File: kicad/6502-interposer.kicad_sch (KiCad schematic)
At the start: 6 parts, among them J1 LogicAnalyzer #1, J2 LogicAnalyzer #2, J3 Conn_02x09_Odd_Even, U1 65CE02

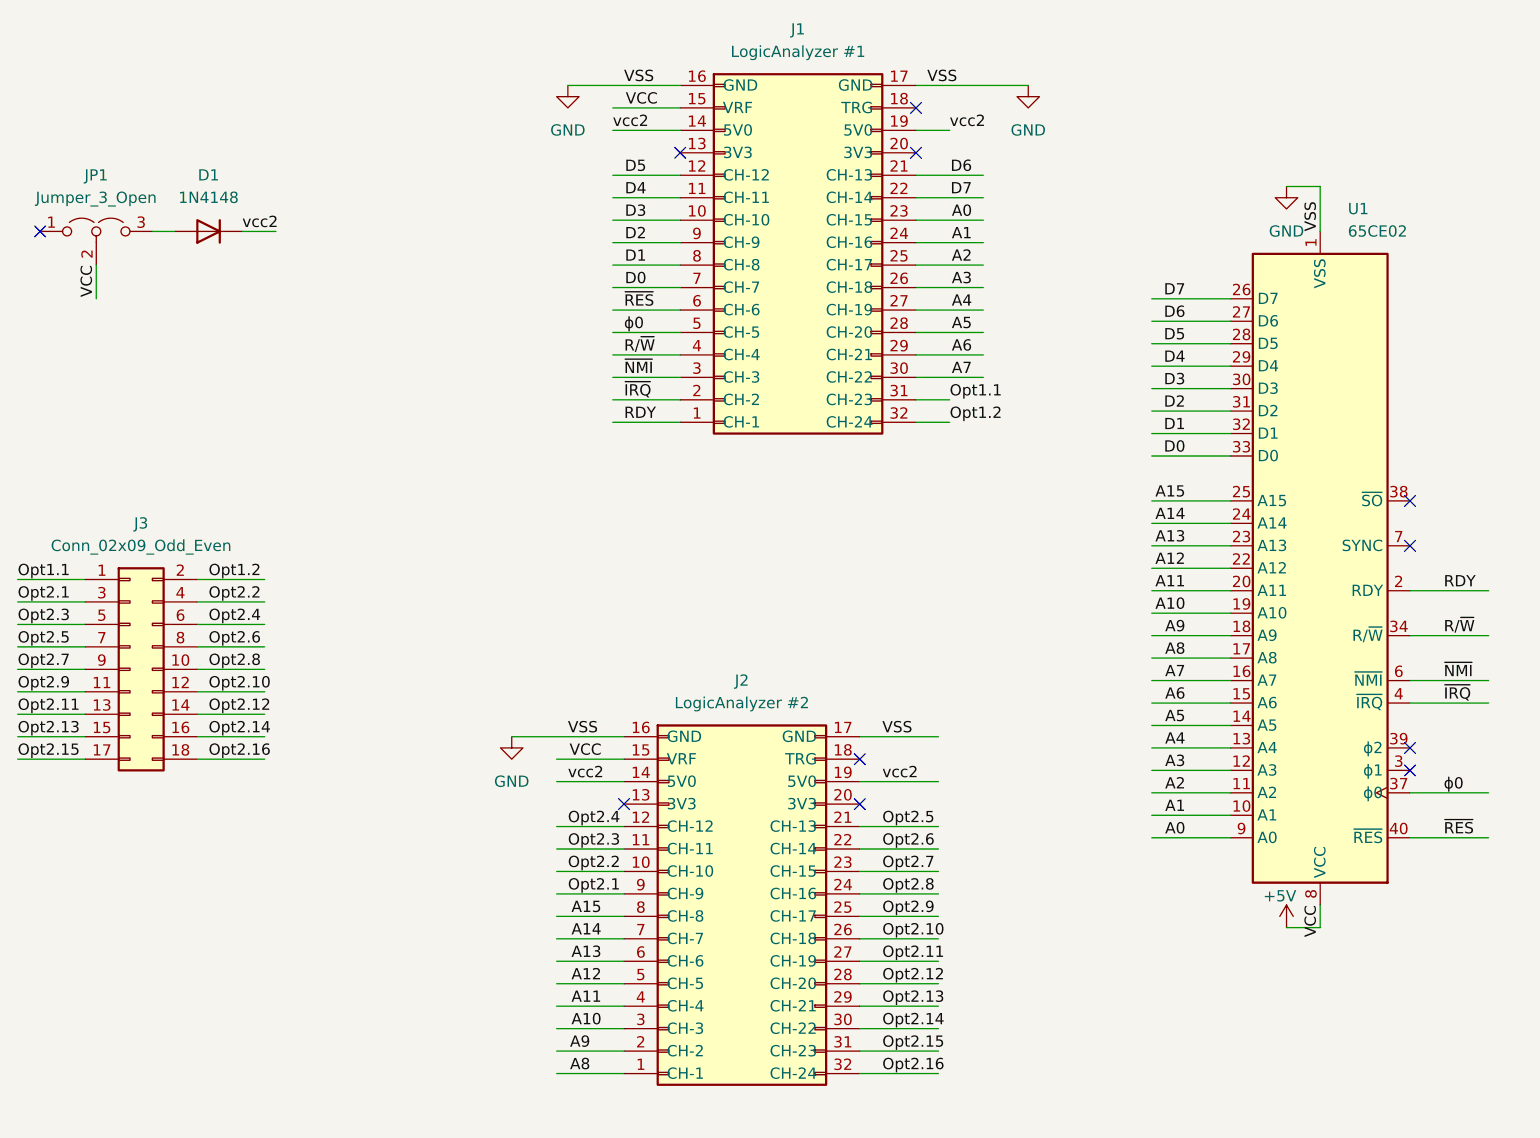
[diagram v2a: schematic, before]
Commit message: Added Phase1 and SYNC
Ended up digging into the 6502 documentation to understand why SYNC and Phase1 are important. Although the IIc and IIe do not use these signals, they do have a function. Sync tells us when the cpu is executing an action, on the system. Phase1 is the inverse of Phase0 or Phase2, and is the time when the Apple II series performs memory actions. Video phase addressing traffic is not visible to the CPU in the Apple II series, the Option ports need to be used to grab those signals. RAn
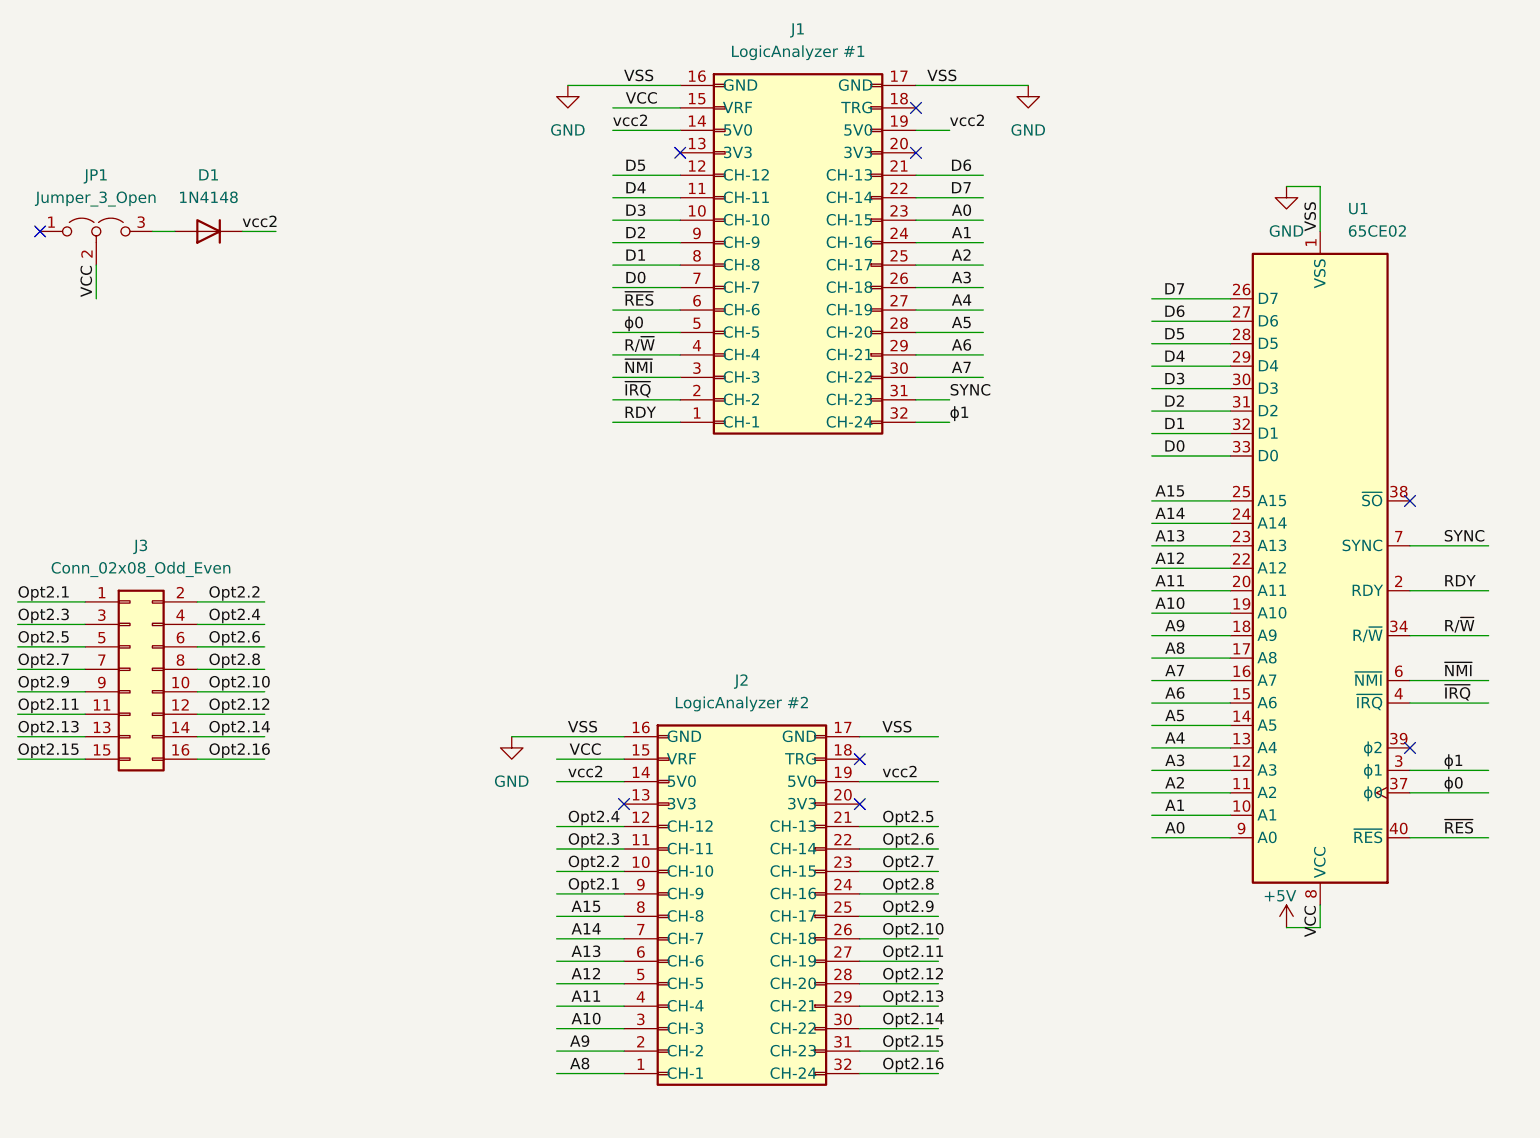
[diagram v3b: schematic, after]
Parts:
- J3: value Conn_02x09_Odd_Even -> Conn_02x08_Odd_Even; footprint Connector_PinSocket_2.54mm:PinSocket_2x09_P2.54mm_Vertical -> Connector_PinSocket_2.54mm:PinSocket_2x08_P2.54mm_Vertical; symbol Connector_Generic:Conn_02x09_Odd_Even -> Connector_Generic:Conn_02x08_Odd_Even
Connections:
- net Opt2.1: now also J3.1 (Pin_1); no longer J3.3 (Pin_3)
- net Opt2.10: now also J3.10 (Pin_10); no longer J3.12 (Pin_12)
- net Opt2.11: now also J3.11 (Pin_11); no longer J3.13 (Pin_13)
- net Opt2.12: now also J3.12 (Pin_12); no longer J3.14 (Pin_14)
- net Opt2.13: now also J3.13 (Pin_13); no longer J3.15 (Pin_15)
- net Opt2.14: now also J3.14 (Pin_14); no longer J3.16 (Pin_16)
- net Opt2.15: now also J3.15 (Pin_15); no longer J3.17 (Pin_17)
- net Opt2.16: now also J3.16 (Pin_16); no longer J3.18 (Pin_18)
- net Opt2.2: now also J3.2 (Pin_2); no longer J3.4 (Pin_4)
- net Opt2.3: now also J3.3 (Pin_3); no longer J3.5 (Pin_5)
- net Opt2.4: now also J3.4 (Pin_4); no longer J3.6 (Pin_6)
- net Opt2.5: now also J3.5 (Pin_5); no longer J3.7 (Pin_7)
- net Opt2.6: now also J3.6 (Pin_6); no longer J3.8 (Pin_8)
- net Opt2.7: now also J3.7 (Pin_7); no longer J3.9 (Pin_9)
- net Opt2.8: now also J3.8 (Pin_8); no longer J3.10 (Pin_10)
- net Opt2.9: now also J3.9 (Pin_9); no longer J3.11 (Pin_11)
- net ϕ1: now reaches U1.3 (ϕ1)
- net ϕ1: now also J1.32 (CH-24)
- net SYNC: now reaches U1.7 (SYNC)
- net SYNC: now also J1.31 (CH-23)
- removed net Opt1.1: J1.31 (CH-23), J3.1 (Pin_1)
- removed net Opt1.2: J1.32 (CH-24), J3.2 (Pin_2)
- no-connect marks 11 -> 9
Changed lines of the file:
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@@
-	)
-	(no_connect
-		(at 201.93 86.36)
 	)
 	(no_connect
@@
 	)
 	(no_connect
-		(at 201.93 111.76)
-	)
-	(no_connect
 		(at 139.7 115.57)
 	)
@@
 	(wire
 		(pts
+			(xy 201.93 86.36) (xy 210.82 86.36)
+		)
+		(stroke
+			(width 0)
+			(type default)
+		)
+	)
+	(wire
+		(pts
 			(xy 64.77 105.41) (xy 72.39 105.41)
 		)
@@
 	(wire
 		(pts
-			(xy 44.45 90.17) (xy 52.07 90.17)
-		)
-		(stroke
-			(width 0)
-			(type default)
-		)
-	)
-	(wire
-		(pts
 			(xy 113.03 128.27) (xy 105.41 128.27)
 		)
@@
 	(wire
 		(pts
+			(xy 201.93 111.76) (xy 210.82 111.76)
+		)
+		(stroke
+			(width 0)
+			(type default)
+		)
+	)
+	(wire
+		(pts
 			(xy 172.72 63.5) (xy 181.61 63.5)
 		)
@@
 		(pts
 			(xy 119.38 69.85) (xy 111.76 69.85)
-		)
-		(stroke
-			(width 0)
-			(type default)
-		)
-	)
-	(wire
-		(pts
-			(xy 64.77 90.17) (xy 72.39 90.17)
 		)
 		(stroke
@@
 		)
 	)
+	(label "SYNC"
+		(at 205.74 86.36 0)
+		(effects
+			(font
+				(size 1.27 1.27)
+			)
+			(justify left bottom)
+		)
+	)
 	(label "D2"
 		(at 176.53 71.12 180)
@@
 		)
 	)
+	(label "ϕ1"
+		(at 205.74 111.76 0)
+		(effects
+			(font
+				(size 1.27 1.27)
+			)
+			(justify left bottom)
+		)
+	)
 	(label "A14"
 		(at 110.49 130.81 180)
@@
 		)
 	)
-	(label "Opt1.2"
+	(label "ϕ1"
 		(at 149.86 72.39 0)
 		(effects
@@
 		)
 	)
-	(label "Opt1.1"
+	(label "SYNC"
 		(at 149.86 69.85 0)
 		(effects
@@
 		)
 	)
-	(label "Opt1.1"
-		(at 44.45 90.17 0)
-		(effects
-			(font
-				(size 1.27 1.27)
-			)
-			(justify left bottom)
-		)
-	)
 	(label "Opt2.3"
 		(at 44.45 95.25 0)
@@
 	(label "Opt2.8"
 		(at 66.04 100.33 0)
-		(effects
-			(font
-				(size 1.27 1.27)
-			)
-			(justify left bottom)
-		)
-	)
-	(label "Opt1.2"
-		(at 66.04 90.17 0)
 		(effects
 			(font
@@
 	)
 	(symbol
-		(lib_id "Connector_Generic:Conn_02x09_Odd_Even")
+		(lib_id "Connector_Generic:Conn_02x08_Odd_Even")
 		(at 57.15 100.33 0)
 		(unit 1)
@@
 		(fields_autoplaced yes)
 		(property "Reference" "J3"
-			(at 58.42 83.82 0)
-			(effects
-				(font
-					(size 1.27 1.27)
-				)
-			)
-		)
-		(property "Value" "Conn_02x09_Odd_Even"
 			(at 58.42 86.36 0)
 			(effects
@@
 			)
 		)
-		(property "Footprint" "Connector_PinSocket_2.54mm:PinSocket_2x09_P2.54mm_Vertical"
+		(property "Value" "Conn_02x08_Odd_Even"
+			(at 58.42 88.9 0)
+			(effects
+				(font
+					(size 1.27 1.27)
+				)
+			)
+		)
+		(property "Footprint" "Connector_PinSocket_2.54mm:PinSocket_2x08_P2.54mm_Vertical"
 			(at 57.15 100.33 0)
 			(effects
@@
 			)
 		)
-		(property "Description" "Generic connector, double row, 02x09, odd/even pin numbering scheme (row 1 odd numbers, row 2 even numbers), script generated (kicad-library-utils/schlib/autogen/connector/)"
+		(property "Description" "Generic connector, double row, 02x08, odd/even pin numbering scheme (row 1 odd numbers, row 2 even numbers), script generated (kicad-library-utils/schlib/autogen/connector/)"
 			(at 57.15 100.33 0)
 			(effects
@@
 		(pin "15"
 		)
-		(pin "17"
-		)
 		(pin "2"
 		)
@@
 		(pin "16"
 		)
-		(pin "18"
-		)
 		(pin "5"

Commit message: fixed labels, sync routing
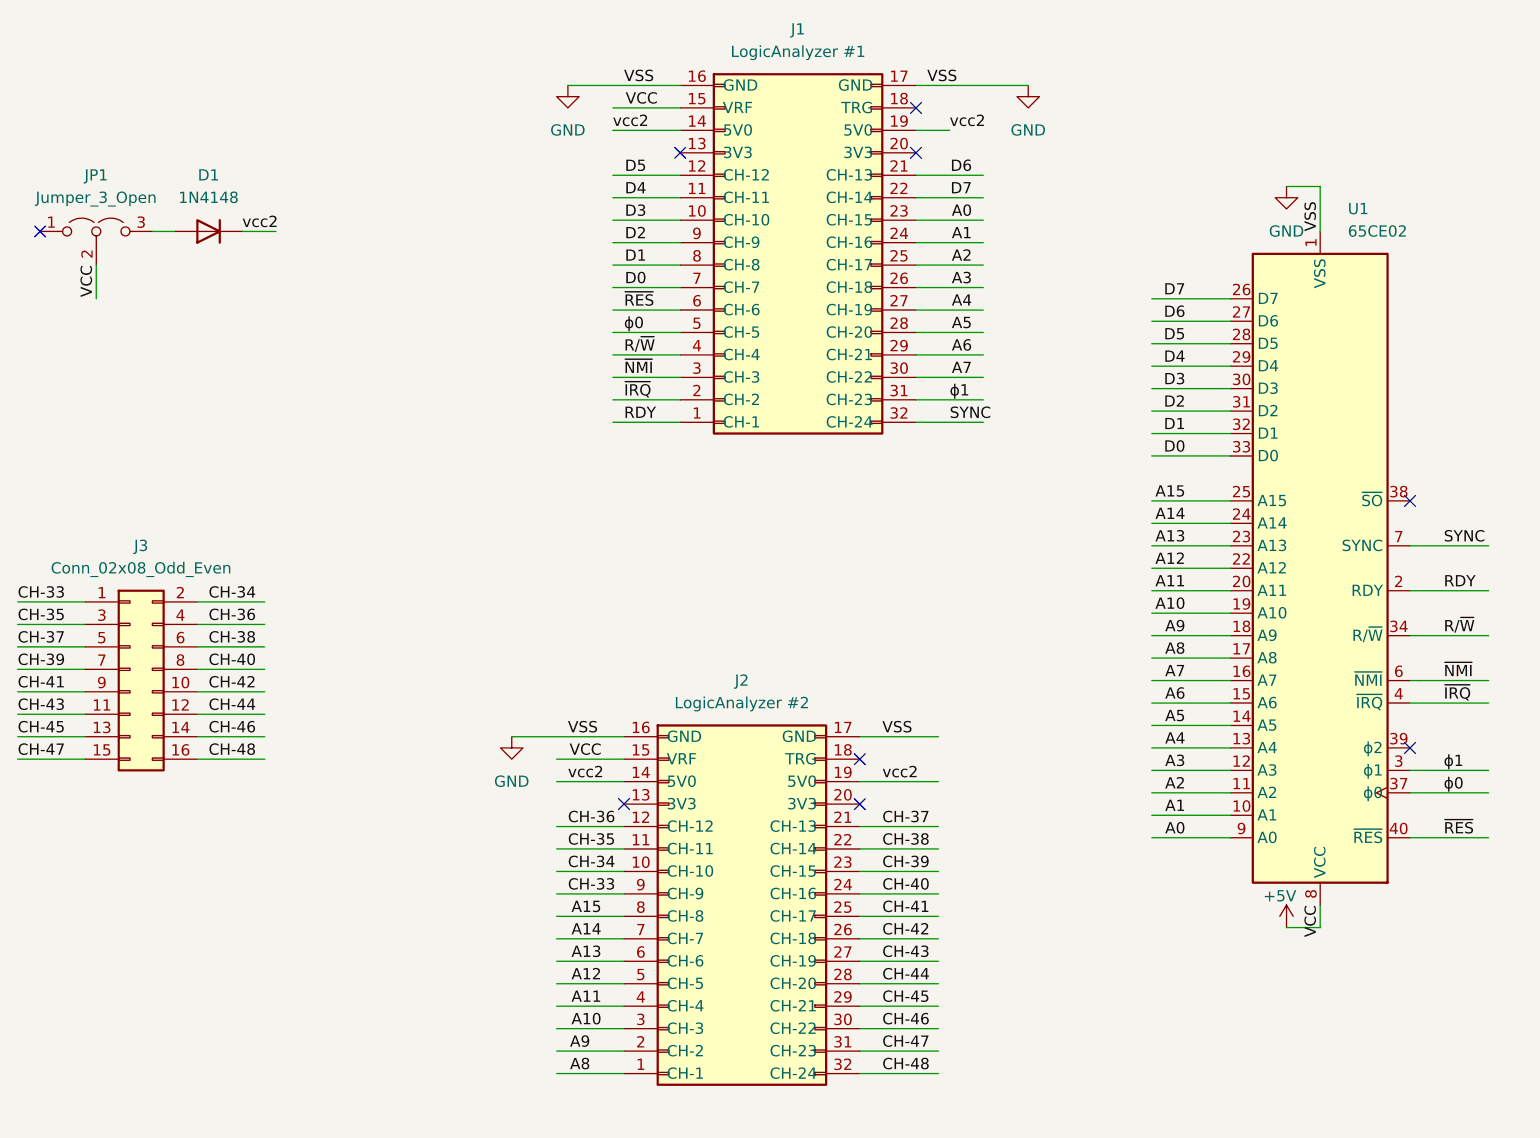
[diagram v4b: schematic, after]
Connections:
- net SYNC: now also J1.32 (CH-24); no longer J1.31 (CH-23)
- net ϕ1: now also J1.31 (CH-23); no longer J1.32 (CH-24)
- net Opt2.1 renamed CH-33
- net Opt2.10 renamed CH-42
- net Opt2.11 renamed CH-43
- net Opt2.12 renamed CH-44
- net Opt2.13 renamed CH-45
- net Opt2.14 renamed CH-46
- net Opt2.15 renamed CH-47
- net Opt2.16 renamed CH-48
- net Opt2.2 renamed CH-34
- net Opt2.3 renamed CH-35
- net Opt2.4 renamed CH-36
- net Opt2.5 renamed CH-37
- net Opt2.6 renamed CH-38
- net Opt2.7 renamed CH-39
- net Opt2.8 renamed CH-40
- net Opt2.9 renamed CH-41
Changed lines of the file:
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@@
-	(wire
-		(pts
-			(xy 146.05 72.39) (xy 149.86 72.39)
-		)
-		(stroke
-			(width 0)
-			(type default)
-		)
-	)
 	(wire
 		(pts
@@
 	(wire
 		(pts
-			(xy 146.05 69.85) (xy 149.86 69.85)
+			(xy 146.05 69.85) (xy 153.67 69.85)
 		)
 		(stroke
@@
 		(pts
 			(xy 59.69 50.8) (xy 62.23 50.8)
+		)
+		(stroke
+			(width 0)
+			(type default)
+		)
+	)
+	(wire
+		(pts
+			(xy 146.05 72.39) (xy 153.67 72.39)
 		)
 		(stroke
@@
 		)
 	)
-	(label "Opt2.6"
+	(label "CH-38"
 		(at 142.24 120.65 0)
 		(effects
@@
 		)
 	)
-	(label "Opt2.10"
+	(label "CH-42"
 		(at 66.04 102.87 0)
 		(effects
@@
 		)
 	)
-	(label "Opt2.13"
+	(label "CH-45"
 		(at 44.45 107.95 0)
 		(effects
@@
 		)
 	)
+	(label "ϕ1"
+		(at 149.86 69.85 0)
+		(effects
+			(font
+				(size 1.27 1.27)
+			)
+			(justify left bottom)
+		)
+	)
 	(label "A11"
 		(at 176.53 91.44 180)
@@
 		)
 	)
-	(label "Opt2.16"
+	(label "CH-48"
 		(at 66.04 110.49 0)
+		(effects
+			(font
+				(size 1.27 1.27)
+			)
+			(justify left bottom)
+		)
+	)
+	(label "SYNC"
+		(at 149.86 72.39 0)
 		(effects
 			(font
@@
 		)
 	)
-	(label "Opt2.13"
+	(label "CH-45"
 		(at 142.24 138.43 0)
 		(effects
@@
 		)
 	)
-	(label "Opt2.12"
+	(label "CH-44"
 		(at 66.04 105.41 0)
 		(effects
@@
 		)
 	)
-	(label "Opt2.15"
+	(label "CH-47"
 		(at 44.45 110.49 0)
 		(effects
@@
 		)
 	)
-	(label "ϕ1"
-		(at 149.86 72.39 0)
-		(effects
-			(font
-				(size 1.27 1.27)
-			)
-			(justify left bottom)
-		)
-	)
 	(label "VCC"
 		(at 116.84 36.83 180)
@@
 		)
 	)
-	(label "Opt2.2"
+	(label "CH-34"
 		(at 106.68 123.19 0)
 		(effects
@@
 		)
 	)
-	(label "Opt2.11"
+	(label "CH-43"
 		(at 142.24 133.35 0)
 		(effects
@@
 		)
 	)
-	(label "Opt2.11"
+	(label "CH-43"
 		(at 44.45 105.41 0)
 		(effects
@@
 		)
 	)
-	(label "Opt2.14"
+	(label "CH-46"
 		(at 142.24 140.97 0)
 		(effects
@@
 		)
 	)
-	(label "Opt2.4"
+	(label "CH-36"
 		(at 106.68 118.11 0)
 		(effects
@@
 		)
 	)
-	(label "Opt2.10"
+	(label "CH-42"
 		(at 142.24 130.81 0)
 		(effects
@@
 		)
 	)
-	(label "Opt2.5"
+	(label "CH-37"
 		(at 142.24 118.11 0)
 		(effects
@@
 		)
 	)
-	(label "Opt2.4"
+	(label "CH-36"
 		(at 66.04 95.25 0)
 		(effects
@@
 		)
 	)
-	(label "Opt2.3"
+	(label "CH-35"
 		(at 106.68 120.65 0)
 		(effects
@@
 		)
 	)
-	(label "Opt2.15"
+	(label "CH-47"
 		(at 142.24 143.51 0)
 		(effects
@@
 		)
 	)
-	(label "Opt2.9"
+	(label "CH-41"
 		(at 142.24 128.27 0)
 		(effects
@@
 		)
 	)
-	(label "Opt2.16"
+	(label "CH-48"
 		(at 142.24 146.05 0)
 		(effects
@@
 		)
 	)
-	(label "Opt2.1"
+	(label "CH-33"
 		(at 106.68 125.73 0)
 		(effects
@@
 		)
 	)
-	(label "Opt2.14"
+	(label "CH-46"
 		(at 66.04 107.95 0)
 		(effects
@@
 		)
 	)
-	(label "Opt2.5"
+	(label "CH-37"
 		(at 44.45 97.79 0)
 		(effects
@@
 		)
 	)
-	(label "Opt2.9"
+	(label "CH-41"
 		(at 44.45 102.87 0)
 		(effects
@@
 		)
 	)
-	(label "Opt2.6"
+	(label "CH-38"
 		(at 66.04 97.79 0)
 		(effects
@@
 		)
 	)
-	(label "Opt2.7"
+	(label "CH-39"
 		(at 44.45 100.33 0)
 		(effects
@@
 		)
 	)
-	(label "Opt2.1"
+	(label "CH-33"
 		(at 44.45 92.71 0)
-		(effects
-			(font
-				(size 1.27 1.27)
-			)
-			(justify left bottom)
-		)
-	)
-	(label "SYNC"
-		(at 149.86 69.85 0)
 		(effects
 			(font
@@
 		)
 	)
-	(label "Opt2.7"
+	(label "CH-39"
 		(at 142.24 123.19 0)
 		(effects
@@
 		)
 	)
-	(label "Opt2.2"
+	(label "CH-34"
 		(at 66.04 92.71 0)
 		(effects
@@
 		)
 	)
-	(label "Opt2.3"
+	(label "CH-35"
 		(at 44.45 95.25 0)
 		(effects
@@
 		)
 	)
-	(label "Opt2.8"
+	(label "CH-40"
 		(at 66.04 100.33 0)
 		(effects
@@
 		)
 	)
-	(label "Opt2.8"
+	(label "CH-40"
 		(at 142.24 125.73 0)
 		(effects
@@
 		)
 	)
-	(label "Opt2.12"
+	(label "CH-44"
 		(at 142.24 135.89 0)
 		(effects
